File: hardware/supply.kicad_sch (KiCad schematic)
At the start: 34 parts, among them U11 LMR38010SDDAR, U2 4011, U3 4081, U4 4071, U7 LM1117-3.3

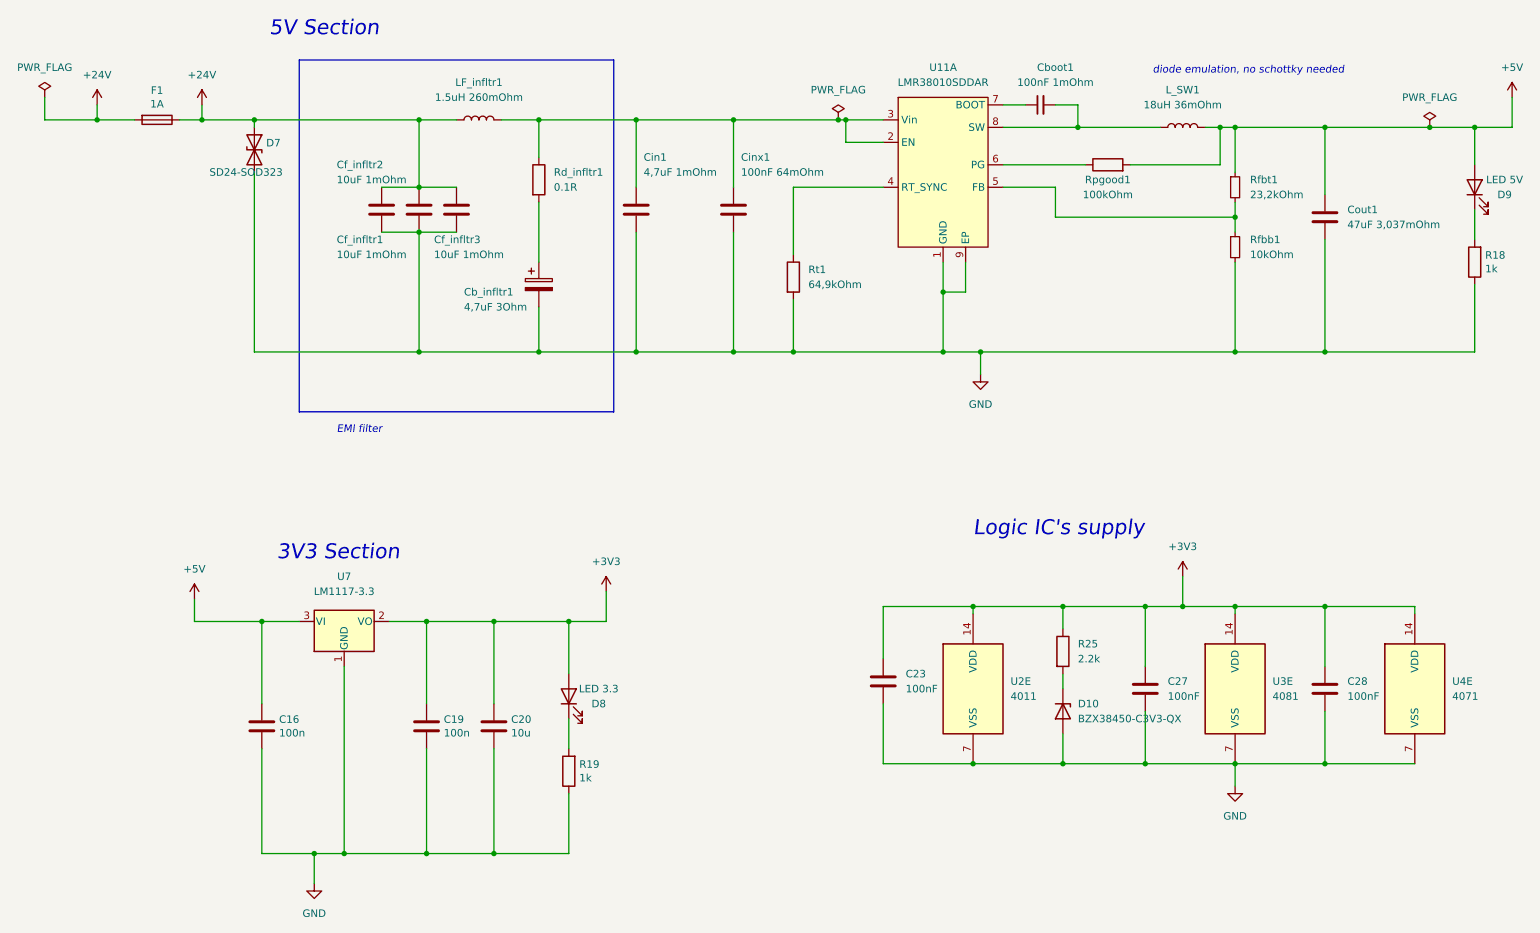
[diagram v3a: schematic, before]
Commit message: routing update, new supply section routed
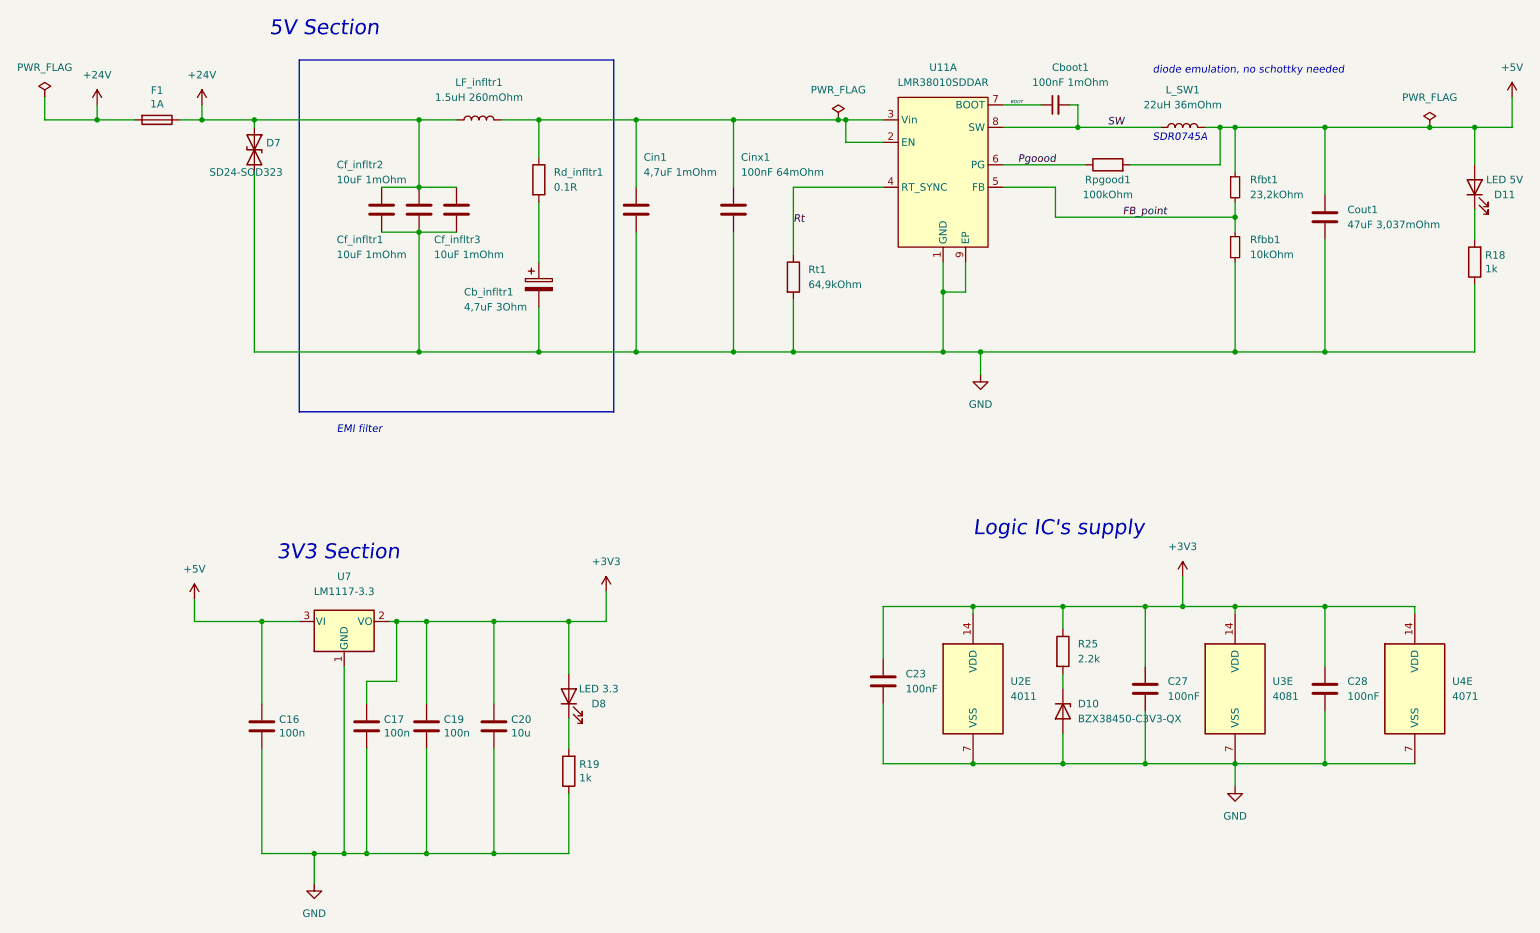
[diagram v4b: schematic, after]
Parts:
- added C17: 100n, Capacitor_SMD:C_0603_1608Metric_Pad1.08x0.95mm_HandSolder, symbol Device:C
- L_SW1: value 18uH 36mOhm -> 22uH 36mOhm
- renumbered D9 to D11
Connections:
- net +3V3: now also C17.1
- net GND: now also C17.2
- net Rt: now reaches Rt1.1, U11.4 (RT_SYNC)
- net FB_point: now reaches Rfbb1.1, Rfbt1.2, U11.5 (FB)
- net Pgoood: now reaches Rpgood1.1, U11.6 (PG)
- net BOOT: now reaches Cboot1.1, U11.7 (BOOT)
- net SW: now reaches Cboot1.2, L_SW1.1, U11.8 (SW)
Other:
- note added: "SDR0745A"
- moved on the sheet: Cboot1
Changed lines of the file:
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@@
   (junction (at 58.42 35.56) (diameter 0) (color 0 0 0 0)
   )
+  (junction (at 77.47 160.02) (diameter 0) (color 0 0 0 0)
+  )
   (junction (at 181.61 74.93) (diameter 0) (color 0 0 0 0)
   )
@@
   (junction (at 224.79 36.83) (diameter 0) (color 0 0 0 0)
   )
+  (junction (at 82.55 120.65) (diameter 0) (color 0 0 0 0)
+  )
   (junction (at 149.86 74.93) (diameter 0) (color 0 0 0 0)
   )
@@
     (stroke (width 0) (type default) (color 0 0 0 0))
   )
+  (wire (pts (xy 77.47 130.81) (xy 82.55 130.81))
+    (stroke (width 0) (type default) (color 0 0 0 0))
+  )
+  (wire (pts (xy 82.55 130.81) (xy 82.55 120.65))
+    (stroke (width 0) (type default) (color 0 0 0 0))
+  )
   (wire (pts (xy 158.75 35.56) (xy 165.1 35.56))
     (stroke (width 0) (type default) (color 0 0 0 0))
@@
     (stroke (width 0) (type default) (color 0 0 0 0))
   )
+  (wire (pts (xy 82.55 120.65) (xy 87.63 120.65))
+    (stroke (width 0) (type default) (color 0 0 0 0))
+  )
   (wire (pts (xy 86.36 46.99) (xy 86.36 35.56))
     (stroke (width 0) (type default) (color 0 0 0 0))
@@
     (stroke (width 0) (type default) (color 0 0 0 0))
   )
-  (wire (pts (xy 81.28 120.65) (xy 87.63 120.65))
+  (wire (pts (xy 81.28 120.65) (xy 82.55 120.65))
     (stroke (width 0) (type default) (color 0 0 0 0))
   )
@@
     (stroke (width 0) (type default) (color 0 0 0 0))
   )
-  (wire (pts (xy 185.42 33.02) (xy 189.23 33.02))
+  (wire (pts (xy 185.42 33.02) (xy 191.77 33.02))
     (stroke (width 0) (type default) (color 0 0 0 0))
   )
@@
     (stroke (width 0) (type default) (color 0 0 0 0))
   )
+  (wire (pts (xy 77.47 134.62) (xy 77.47 130.81))
+    (stroke (width 0) (type default) (color 0 0 0 0))
+  )
   (wire (pts (xy 58.42 35.56) (xy 86.36 35.56))
     (stroke (width 0) (type default) (color 0 0 0 0))
@@
     (stroke (width 0) (type default) (color 0 0 0 0))
   )
+  (wire (pts (xy 77.47 160.02) (xy 87.63 160.02))
+    (stroke (width 0) (type default) (color 0 0 0 0))
+  )
   (wire (pts (xy 118.11 115.57) (xy 118.11 120.65))
     (stroke (width 0) (type default) (color 0 0 0 0))
@@
     (stroke (width 0) (type default) (color 0 0 0 0))
   )
+  (wire (pts (xy 77.47 142.24) (xy 77.47 160.02))
+    (stroke (width 0) (type default) (color 0 0 0 0))
+  )
   (wire (pts (xy 180.34 119.38) (xy 180.34 118.11))
     (stroke (width 0) (type default) (color 0 0 0 0))
@@
     (stroke (width 0) (type default) (color 0 0 0 0))
   )
-  (wire (pts (xy 198.12 33.02) (xy 194.31 33.02))
+  (wire (pts (xy 198.12 33.02) (xy 196.85 33.02))
     (stroke (width 0) (type default) (color 0 0 0 0))
   )
@@
     (stroke (width 0) (type default) (color 0 0 0 0))
   )
-  (wire (pts (xy 73.66 160.02) (xy 87.63 160.02))
+  (wire (pts (xy 73.66 160.02) (xy 77.47 160.02))
     (stroke (width 0) (type default) (color 0 0 0 0))
   )
@@
   (text "5V Section" (at 60.96 21.59 0)
     (effects (font (size 2.54 2.54) italic) (justify left bottom))
+  )
+  (text "SDR0745A\n" (at 210.82 39.37 0)
+    (effects (font (size 1.27 1.27) italic) (justify left bottom))
+  )
+  (label "Pgoood" (at 187.96 43.18 0)
+    (effects (font (size 1.27 1.27) italic) (justify left bottom))
+  )
+  (label "Rt" (at 149.86 53.34 0)
+    (effects (font (size 1.27 1.27) italic) (justify left bottom))
+  )
+  (label "SW" (at 203.2 36.83 0)
+    (effects (font (size 1.27 1.27) italic) (justify left bottom))
+  )
+  (label "FB_point" (at 205.74 52.07 0)
+    (effects (font (size 1.27 1.27) italic) (justify left bottom))
+  )
+  (label "BOOT" (at 186.69 33.02 0)
+    (effects (font (size 0.54 0.54) italic) (justify left bottom))
   )
   (symbol (lib_id "Device:R") (at 265.43 59.69 180) (unit 1)
@@
   (symbol (lib_id "Device:LED") (at 265.43 46.99 90) (unit 1)
     (in_bom yes) (on_board yes)
-    (property "Reference" "D9" (id 0) (at 270.51 48.26 90))
+    (property "Reference" "D11" (id 0) (at 270.51 48.26 90))
     (property "Value" "LED 5V" (id 1) (at 270.51 45.72 90))
     (property "Footprint" "LED_SMD:LED_0603_1608Metric_Pad1.05x0.95mm_HandSolder" (id 2) (at 265.43 46.99 0)
@@
     (pin "2")
   )
+  (symbol (lib_id "Device:C") (at 77.47 138.43 0) (unit 1)
+    (in_bom yes) (on_board yes)
+    (property "Reference" "C17" (id 0) (at 80.391 137.2616 0)
+      (effects (font (size 1.27 1.27)) (justify left))
+    )
+    (property "Value" "100n" (id 1) (at 80.391 139.573 0)
+      (effects (font (size 1.27 1.27)) (justify left))
+    )
+    (property "Footprint" "Capacitor_SMD:C_0603_1608Metric_Pad1.08x0.95mm_HandSolder" (id 2) (at 78.4352 142.24 0)
+      (effects (font (size 1.27 1.27)) hide)
+    )
+    (property "Datasheet" "~" (id 3) (at 77.47 138.43 0)
+      (effects (font (size 1.27 1.27)) hide)
+    )
+    (pin "1")
+    (pin "2")
+  )
   (symbol (lib_id "Device:R_Small") (at 224.79 57.15 0) (unit 1)
     (in_bom yes) (on_board yes) (fields_autoplaced)
@@
     (in_bom yes) (on_board yes) (fields_autoplaced)
     (property "Reference" "L_SW1" (id 0) (at 215.9 30.48 90))
-    (property "Value" "18uH 36mOhm" (id 1) (at 215.9 33.02 90))
+    (property "Value" "22uH 36mOhm" (id 1) (at 215.9 33.02 90))
     (property "Footprint" "PUTM_Kicad_FOOTPRINTS:L_Bourns_EBS" (id 2) (at 215.9 36.83 0)
       (effects (font (size 1.27 1.27)) hide)
@@
     (pin "2")
   )
-  (symbol (lib_id "Device:C_Small") (at 191.77 33.02 90) (unit 1)
-    (in_bom yes) (on_board yes)
-    (property "Reference" "Cboot1" (id 0) (at 194.31 26.67 90))
-    (property "Value" "100nF 1mOhm" (id 1) (at 194.31 29.21 90))
-    (property "Footprint" "Capacitor_SMD:C_0402_1005Metric_Pad0.74x0.62mm_HandSolder" (id 2) (at 191.77 33.02 0)
-      (effects (font (size 1.27 1.27)) hide)
-    )
-    (property "Datasheet" "~" (id 3) (at 191.77 33.02 0)
-      (effects (font (size 1.27 1.27)) hide)
-    )
+  (symbol (lib_id "Device:C_Small") (at 194.31 33.02 90) (unit 1)
+    (in_bom yes) (on_board yes)
+    (property "Reference" "Cboot1" (id 0) (at 196.85 26.67 90))
+    (property "Value" "100nF 1mOhm" (id 1) (at 196.85 29.21 90))
+    (property "Footprint" "Capacitor_SMD:C_0402_1005Metric_Pad0.74x0.62mm_HandSolder" (id 2) (at 194.31 33.02 0)
+      (effects (font (size 1.27 1.27)) hide)
+    )
+    (property "Datasheet" "~" (id 3) (at 194.31 33.02 0)
+      (effects (font (size 1.27 1.27)) hide)
+    )

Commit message: DRC fixes part 1
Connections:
- net +24V: no longer F1.2
- new net 24v input: F1.2
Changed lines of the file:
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@@
     (effects (font (size 0.54 0.54) italic) (justify left bottom))
+  )
+  (global_label "24v input" (shape input) (at 31.75 33.02 90) (fields_autoplaced)
+    (effects (font (size 1.27 1.27)) (justify left))
+    (property "Intersheet References" "${INTERSHEET_REFS}" (id 0) (at 31.8294 21.475 90)
+      (effects (font (size 1.27 1.27)) (justify left) hide)
+    )
   )
   (symbol (lib_id "Device:R") (at 265.43 59.69 180) (unit 1)
@@
     (pin "2")
   )
-  (symbol (lib_id "power:+24V") (at 31.75 33.02 0) (unit 1)
-    (in_bom yes) (on_board yes) (fields_autoplaced)
-    (property "Reference" "#PWR01" (id 0) (at 31.75 36.83 0)
-      (effects (font (size 1.27 1.27)) hide)
-    )
-    (property "Value" "+24V" (id 1) (at 31.75 27.94 0))
-    (property "Footprint" "" (id 2) (at 31.75 33.02 0)
-      (effects (font (size 1.27 1.27)) hide)
-    )
-    (property "Datasheet" "" (id 3) (at 31.75 33.02 0)
-      (effects (font (size 1.27 1.27)) hide)
-    )
-    (pin "1")
-  )
   (symbol (lib_id "4xxx:4071") (at 255.27 132.08 0) (unit 5)
